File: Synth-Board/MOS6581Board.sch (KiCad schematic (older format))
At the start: 52 parts, among them J1 AUDIO_OUT, J10 CLOCK_TP, J2 Power connector, J3 DEBUG_UART, J4 MIDI_IN, J5 JTAG, J6 AUDIO_IN, J7 I2C, J8 GPIO, J9 RW_TP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

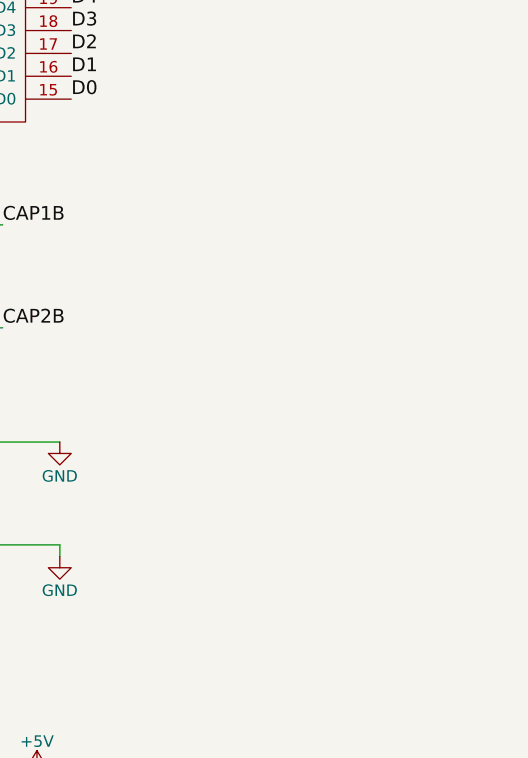
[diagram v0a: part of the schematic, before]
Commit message: added i2c mux to synth board.
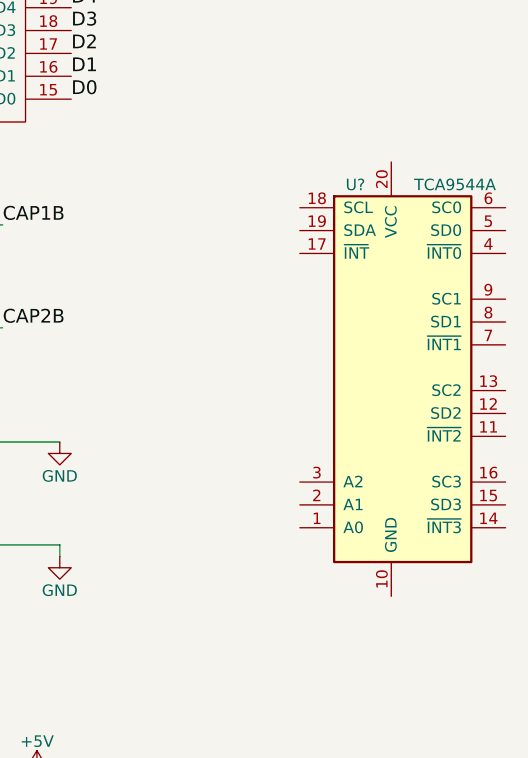
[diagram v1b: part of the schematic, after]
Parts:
- added U?: TCA9544A, Housings_SSOP:TSSOP-20_4.4x6.5mm_Pitch0.65mm, symbol TCA9544A
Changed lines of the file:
@@
 EESchema Schematic File Version 2
-LIBS:MOS6581Board-rescue
 LIBS:power
 LIBS:device
@@
 	0    1    1    0
 $EndComp
+$Comp
+L TCA9544A U?
+U 1 1 5C299205
+P 8800 6375
+F 0 "U?" H 8600 7175 50  0000 L CNN
+F 1 "TCA9544A" H 8900 7175 50  0000 L CNN
+F 2 "Housings_SSOP:TSSOP-20_4.4x6.5mm_Pitch0.65mm" H 9800 5475 50  0001 C CNN
+F 3 "" H 8850 6625 50  0000 C CNN
+	1    8800 6375
+	1    0    0    -1
+$EndComp
 $EndSCHEMATC
